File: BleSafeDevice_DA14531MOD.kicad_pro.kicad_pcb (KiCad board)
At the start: 2 copper layers, 43.5 x 33.5 mm, 19 parts, among them J1 SWD_DEBUG_PADS, J2 CURRENT_MEAS_PADS, SW1 PTS526SK15SMTR2 LFS, U4 DA14531MOD-00F01002

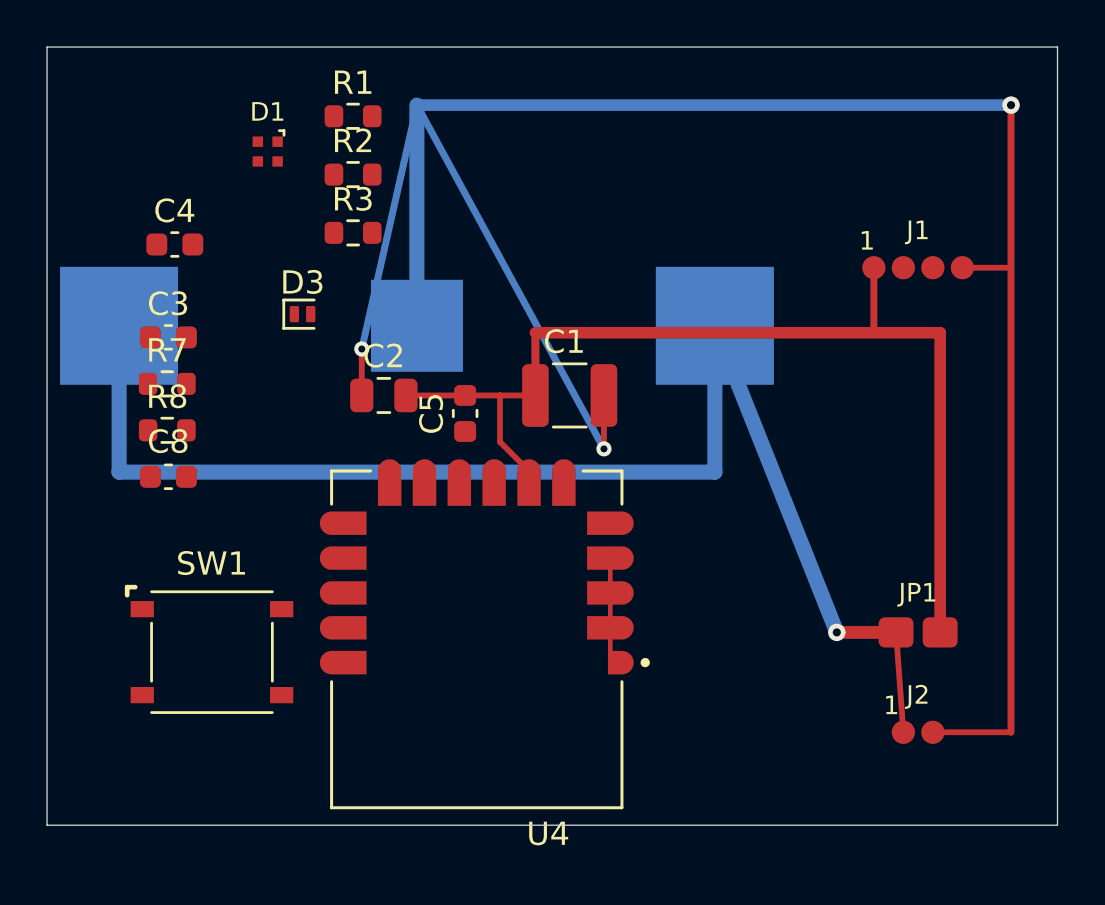
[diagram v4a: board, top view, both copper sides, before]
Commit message: Route DA14531 ground fanout and SWD debug
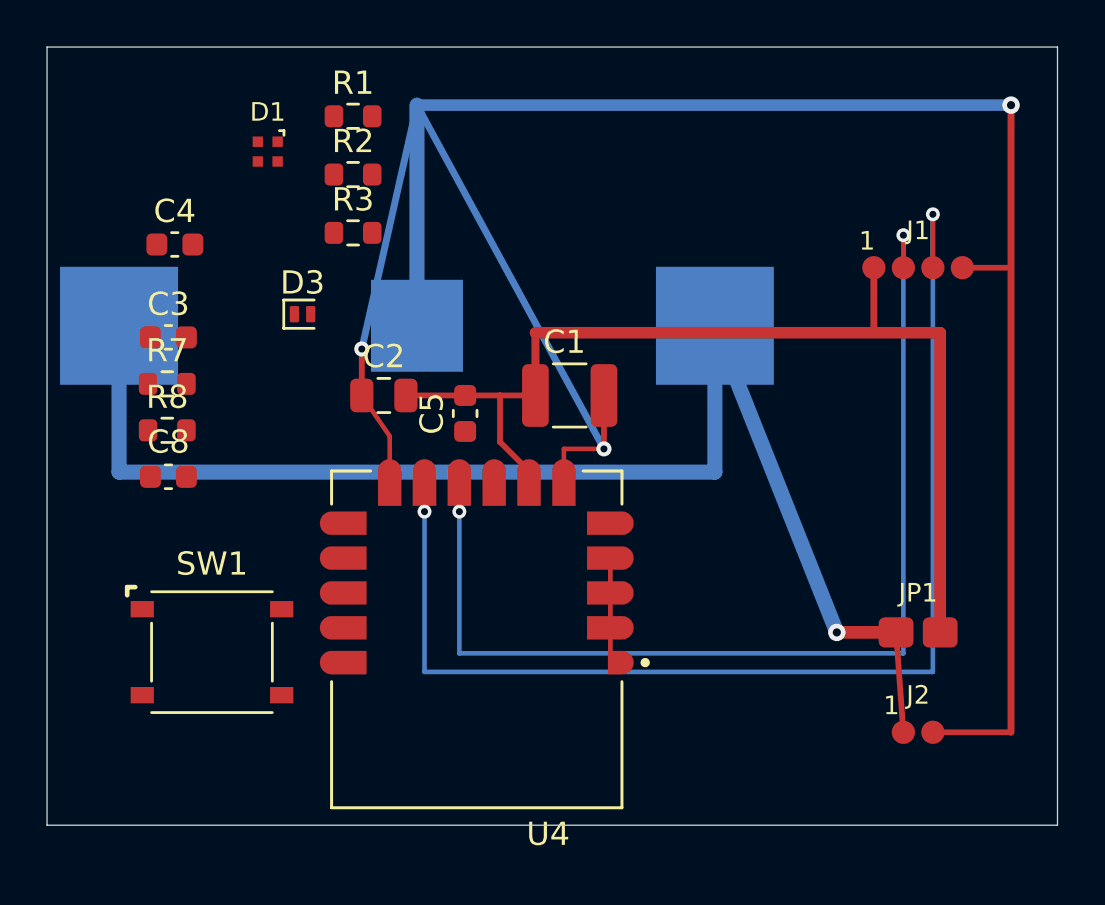
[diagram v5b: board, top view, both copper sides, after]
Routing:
- net /SWCLK: track 0.00 -> 52.0 mm, vias 0 -> 2
- net /SWDIO: track 0.00 -> 45.9 mm, vias 0 -> 2
- net GND: track 103.9 -> 111.2 mm
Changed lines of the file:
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@@
+	)
+	(segment
+		(start 113.75 113.25)
+		(end 112.55 111.5)
+		(width 0.2)
+		(layer "F.Cu")
+		(net 2)
+	)
+	(segment
+		(start 113.75 115.25)
+		(end 113.75 113.25)
+		(width 0.2)
+		(layer "F.Cu")
+		(net 2)
 	)
 	(segment
@@
 		(end 140.5 126)
 		(width 0.3)
+		(layer "F.Cu")
+		(net 2)
+	)
+	(segment
+		(start 121.25 115.25)
+		(end 121.25 113.8)
+		(width 0.2)
+		(layer "F.Cu")
+		(net 2)
+	)
+	(segment
+		(start 121.25 113.8)
+		(end 122.975 113.8)
+		(width 0.2)
 		(layer "F.Cu")
 		(net 2)
@@
 		(net 3)
 	)
+	(segment
+		(start 115.25 115.25)
+		(end 115.25 116.5)
+		(width 0.2)
+		(layer "F.Cu")
+		(net 9)
+	)
+	(segment
+		(start 137.135 103.7)
+		(end 137.135 106)
+		(width 0.2)
+		(layer "F.Cu")
+		(net 9)
+	)
+	(via
+		(at 115.25 116.5)
+		(size 0.6)
+		(drill 0.3)
+		(layers "F.Cu" "B.Cu")
+		(net 9)
+	)
+	(via
+		(at 137.135 103.7)
+		(size 0.6)
+		(drill 0.3)
+		(layers "F.Cu" "B.Cu")
+		(net 9)
+	)
+	(segment
+		(start 115.25 116.5)
+		(end 115.25 123.4)
+		(width 0.2)
+		(layer "B.Cu")
+		(net 9)
+	)
+	(segment
+		(start 115.25 123.4)
+		(end 137.135 123.4)
+		(width 0.2)
+		(layer "B.Cu")
+		(net 9)
+	)
+	(segment
+		(start 137.135 123.4)
+		(end 137.135 103.7)
+		(width 0.2)
+		(layer "B.Cu")
+		(net 9)
+	)
+	(segment
+		(start 116.75 115.25)
+		(end 116.75 116.5)
+		(width 0.2)
+		(layer "F.Cu")
+		(net 10)
+	)
+	(segment
+		(start 135.865 104.6)
+		(end 135.865 106)
+		(width 0.2)
+		(layer "F.Cu")
+		(net 10)
+	)
+	(via
+		(at 135.865 104.6)
+		(size 0.6)
+		(drill 0.3)
+		(layers "F.Cu" "B.Cu")
+		(net 10)
+	)
+	(via
+		(at 116.75 116.5)
+		(size 0.6)
+		(drill 0.3)
+		(layers "F.Cu" "B.Cu")
+		(net 10)
+	)
+	(segment
+		(start 116.75 116.5)
+		(end 116.75 122.6)
+		(width 0.2)
+		(layer "B.Cu")
+		(net 10)
+	)
+	(segment
+		(start 116.75 122.6)
+		(end 135.865 122.6)
+		(width 0.2)
+		(layer "B.Cu")
+		(net 10)
+	)
+	(segment
+		(start 135.865 122.6)
+		(end 135.865 104.6)
+		(width 0.2)
+		(layer "B.Cu")
+		(net 10)
+	)
 	(zone

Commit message: Replan PCB placement for button and LED routing
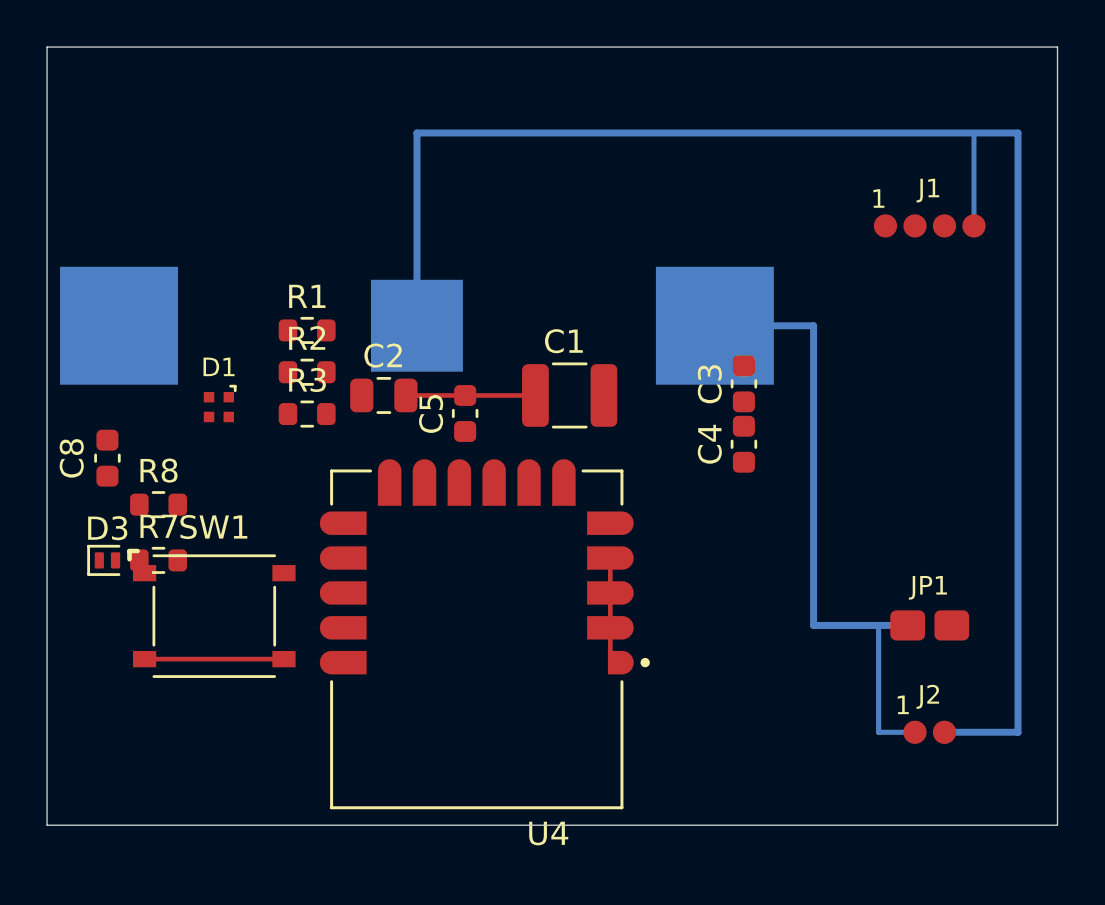
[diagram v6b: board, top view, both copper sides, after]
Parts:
- moved C4 26.0 mm to (129.0, 113.6), turned to 90 degrees
- moved C3 24.9 mm to (129.0, 111.0), turned to 90 degrees
- moved D3 13.5 mm to (101.6, 118.6)
- moved D1 11.2 mm to (106.4, 112.0)
- moved R1 9.43 mm to (110.2, 108.7)
- moved R2 8.74 mm to (110.2, 110.5)
- moved R3 8.05 mm to (110.2, 112.3)
- moved R7 7.61 mm to (103.8, 118.6)
- moved R8 3.22 mm to (103.8, 116.2)
- moved C8 2.74 mm to (101.6, 114.2), turned to 90 degrees
- moved J1 1.87 mm to (137.0, 104.2)
- moved SW1 1.55 mm to (106.2, 121.0)
- moved JP1 0.58 mm to (137.0, 121.4)
- moved J2 0.50 mm to (137.0, 126.0)
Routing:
- net /SWCLK: track 52.0 -> 0.00 mm, vias 2 -> 0
- net /SWDIO: track 45.9 -> 0.00 mm, vias 2 -> 0
- net VCC: track 44.3 -> 5.58 mm
- net GND: track 111.2 -> 79.5 mm, vias 3 -> 0
- net VBAT: track 59.3 -> 28.6 mm, vias 1 -> 0

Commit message: Restore power and ground routing after layout replan
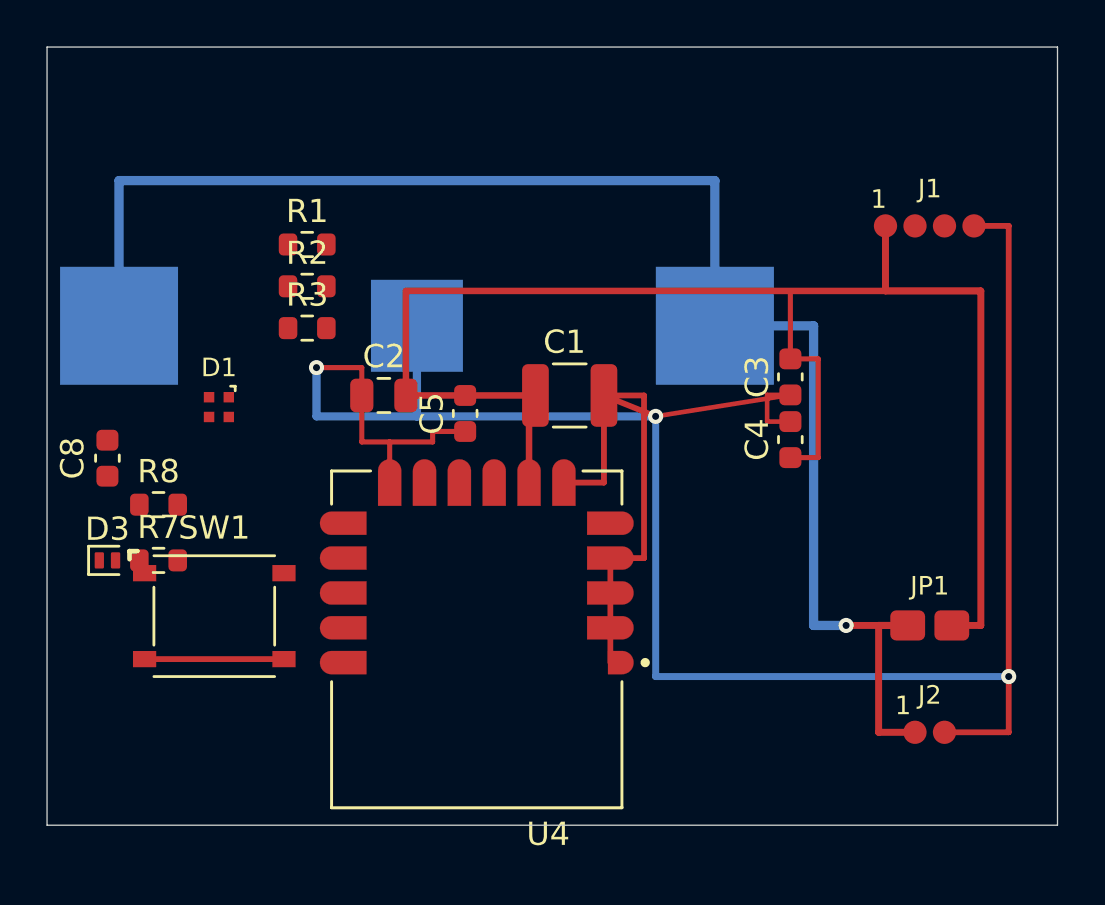
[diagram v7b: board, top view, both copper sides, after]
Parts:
- moved R1 3.70 mm to (110.2, 105.0)
- moved R2 3.70 mm to (110.2, 106.8)
- moved R3 3.70 mm to (110.2, 108.6)
- moved C3 2.02 mm to (131.0, 110.7)
- moved C4 2.01 mm to (131.0, 113.4)
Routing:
- net VCC: track 5.58 -> 79.2 mm
- net GND: track 79.5 -> 126.3 mm, vias 0 -> 3
- net VBAT: track 28.6 -> 66.8 mm, vias 0 -> 1

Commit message: Route SWD and button network
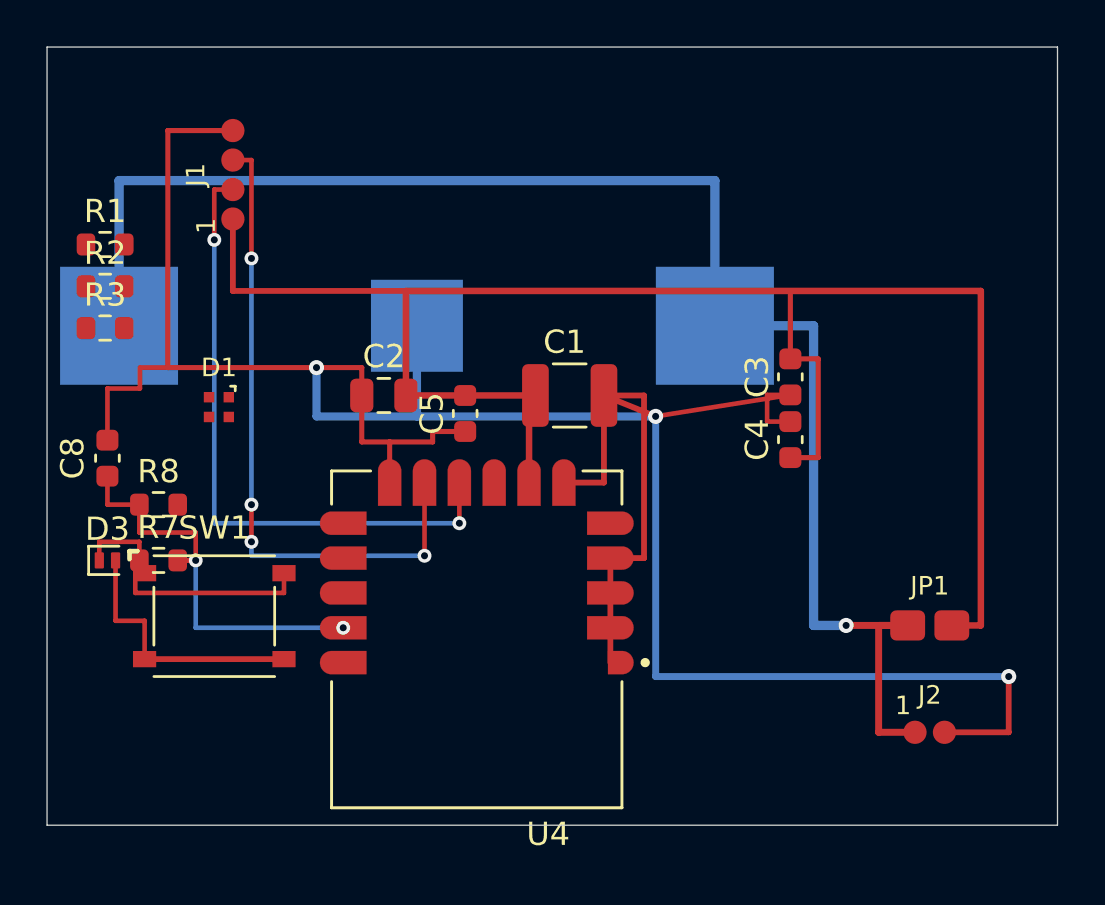
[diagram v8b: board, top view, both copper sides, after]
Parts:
- moved J1 30.1 mm to (107.0, 102.0), turned to 90 degrees
- moved R1 8.70 mm to (101.5, 105.0)
- moved R2 8.70 mm to (101.5, 106.8)
- moved R3 8.70 mm to (101.5, 108.6)
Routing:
- net /SWCLK: track 0.00 -> 28.4 mm, vias 0 -> 4
- net /SWDIO: track 0.00 -> 27.5 mm, vias 0 -> 2
- net /BTN_SW: track 0.00 -> 18.2 mm, vias 0 -> 2
- net Net-(D3-K): track 0.00 -> 12.7 mm
- net GND: track 126.3 -> 136.1 mm
- net VCC: track 79.2 -> 82.8 mm
